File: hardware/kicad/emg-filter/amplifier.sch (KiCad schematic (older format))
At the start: 40 parts, among them U51 LM4565, U52 LM4565, U53 LM4565, U54 LM4565, U55 LM4565, U56 LM4565, U57 LM4565, U58 LM4565

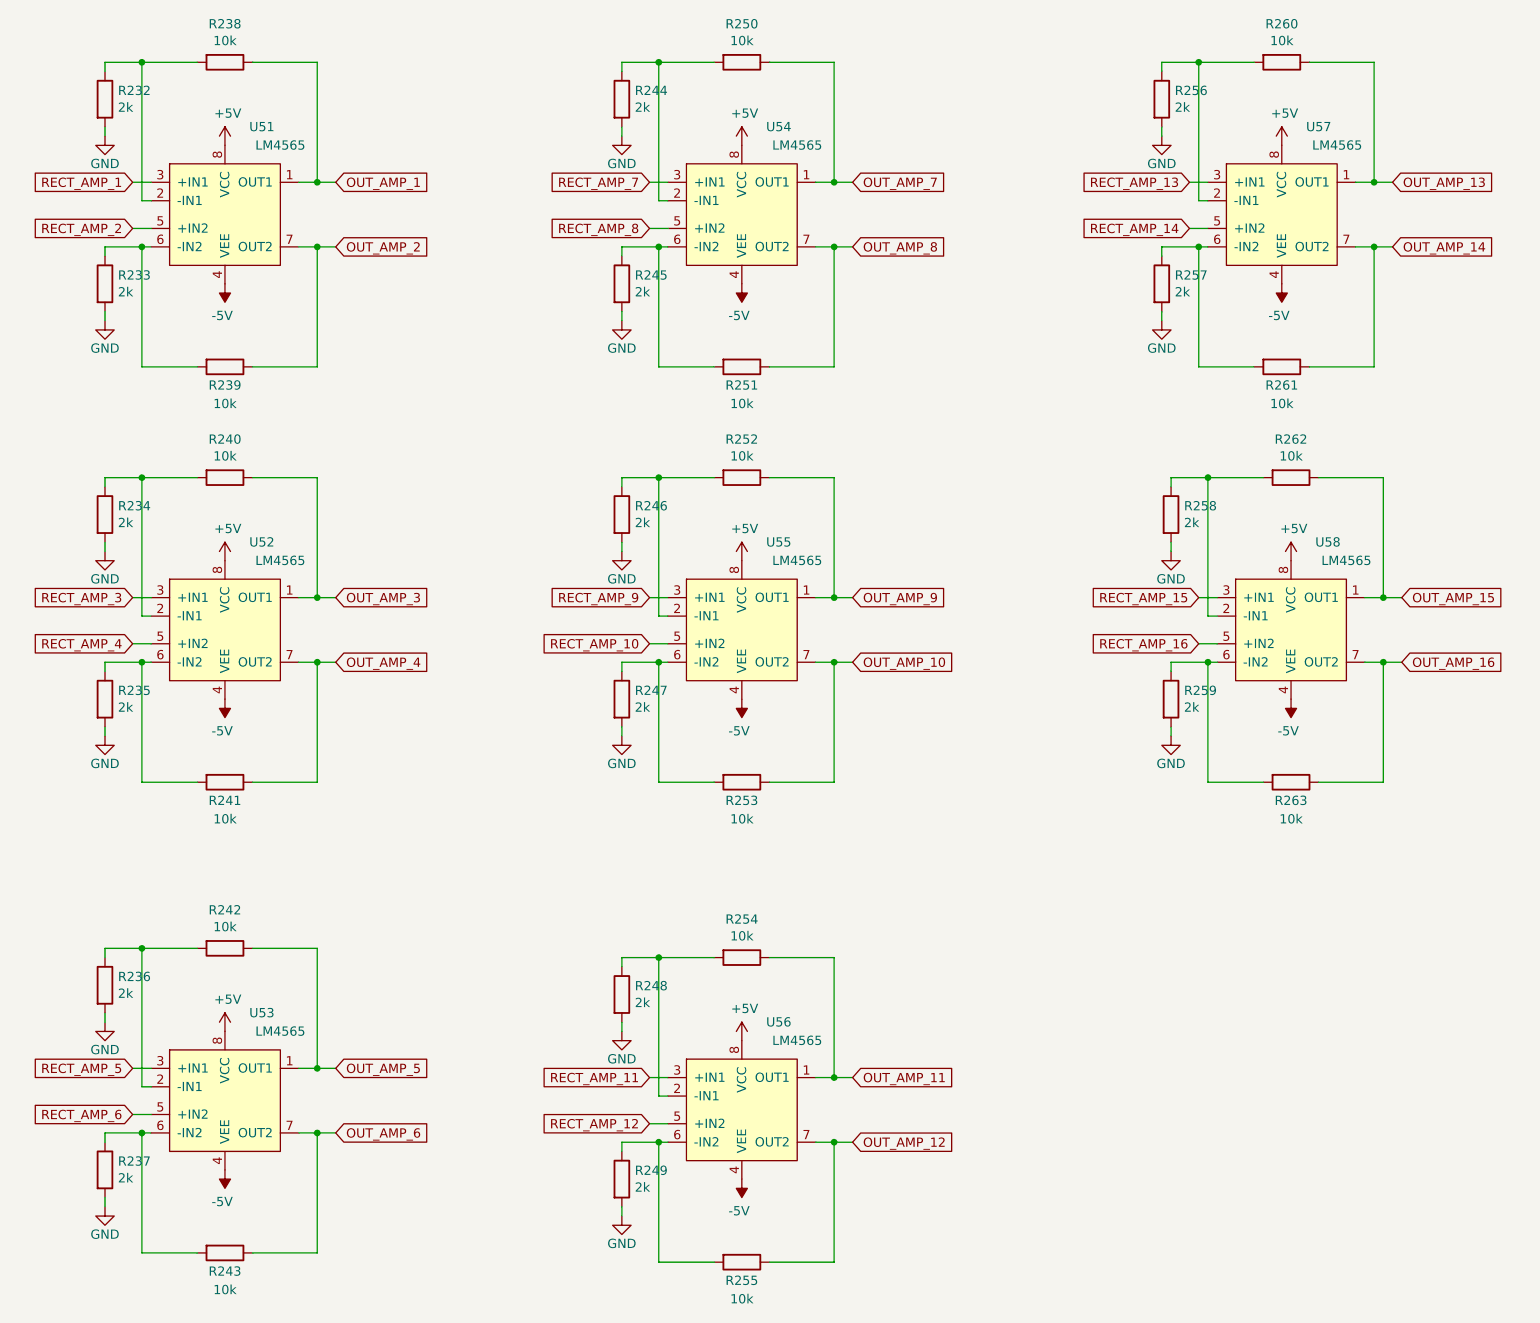
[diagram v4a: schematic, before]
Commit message: footprint association
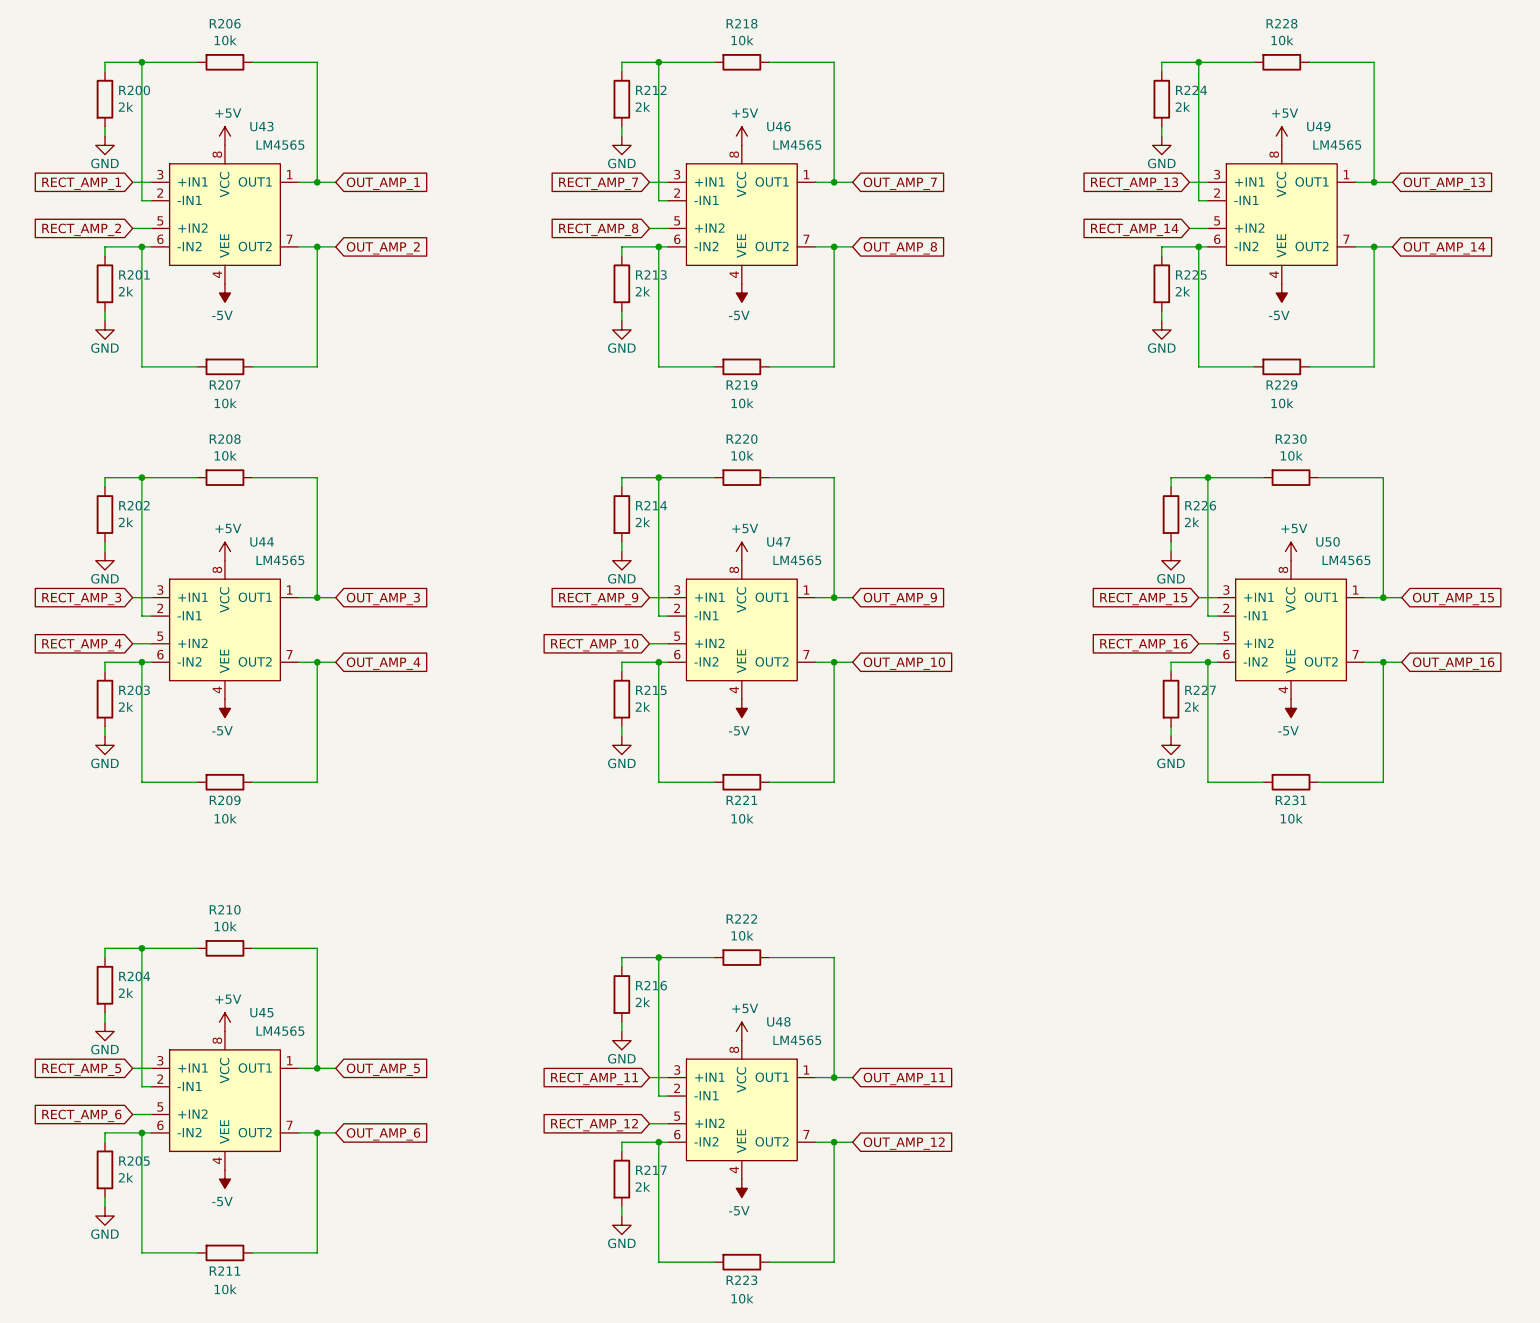
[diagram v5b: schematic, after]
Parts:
- R200: renamed from R232; footprint (none) -> Resistor_SMD:R_0805_2012Metric
- R201: renamed from R233; footprint (none) -> Resistor_SMD:R_0805_2012Metric
- R202: renamed from R234; footprint (none) -> Resistor_SMD:R_0805_2012Metric
- R203: renamed from R235; footprint (none) -> Resistor_SMD:R_0805_2012Metric
- R204: renamed from R236; footprint (none) -> Resistor_SMD:R_0805_2012Metric
- R205: renamed from R237; footprint (none) -> Resistor_SMD:R_0805_2012Metric
- R206: renamed from R238; footprint (none) -> Resistor_SMD:R_0805_2012Metric
- R207: renamed from R239; footprint (none) -> Resistor_SMD:R_0805_2012Metric
- R208: renamed from R240; footprint (none) -> Resistor_SMD:R_0805_2012Metric
- R209: renamed from R241; footprint (none) -> Resistor_SMD:R_0805_2012Metric
- R210: renamed from R242; footprint (none) -> Resistor_SMD:R_0805_2012Metric
- R211: renamed from R243; footprint (none) -> Resistor_SMD:R_0805_2012Metric
- R212: renamed from R244; footprint (none) -> Resistor_SMD:R_0805_2012Metric
- R213: renamed from R245; footprint (none) -> Resistor_SMD:R_0805_2012Metric
- R214: renamed from R246; footprint (none) -> Resistor_SMD:R_0805_2012Metric
- R215: renamed from R247; footprint (none) -> Resistor_SMD:R_0805_2012Metric
- R216: renamed from R248; footprint (none) -> Resistor_SMD:R_0805_2012Metric
- R217: renamed from R249; footprint (none) -> Resistor_SMD:R_0805_2012Metric
- R218: renamed from R250; footprint (none) -> Resistor_SMD:R_0805_2012Metric
- R219: renamed from R251; footprint (none) -> Resistor_SMD:R_0805_2012Metric
- R220: renamed from R252; footprint (none) -> Resistor_SMD:R_0805_2012Metric
- R221: renamed from R253; footprint (none) -> Resistor_SMD:R_0805_2012Metric
- R222: renamed from R254; footprint (none) -> Resistor_SMD:R_0805_2012Metric
- R223: renamed from R255; footprint (none) -> Resistor_SMD:R_0805_2012Metric
- R224: renamed from R256; footprint (none) -> Resistor_SMD:R_0805_2012Metric
- R225: renamed from R257; footprint (none) -> Resistor_SMD:R_0805_2012Metric
- R226: renamed from R258; footprint (none) -> Resistor_SMD:R_0805_2012Metric
- R227: renamed from R259; footprint (none) -> Resistor_SMD:R_0805_2012Metric
- R228: renamed from R260; footprint (none) -> Resistor_SMD:R_0805_2012Metric
- R229: renamed from R261; footprint (none) -> Resistor_SMD:R_0805_2012Metric
- R230: renamed from R262; footprint (none) -> Resistor_SMD:R_0805_2012Metric
- R231: renamed from R263; footprint (none) -> Resistor_SMD:R_0805_2012Metric
- renumbered U51 to U43, U52 to U44, U53 to U45, U54 to U46, U55 to U47, U56 to U48, U57 to U49, U58 to U50

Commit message: Solving Stuff for Free
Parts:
- renumbered R200 to R232, R201 to R233, R202 to R234, R203 to R235, R204 to R236, R205 to R237, R206 to R238, R207 to R239, R208 to R240, R209 to R241, R210 to R242, R211 to R243, R212 to R244, R213 to R245, R214 to R246, R215 to R247, R216 to R248, R217 to R249, R218 to R250, R219 to R251, R220 to R252, R221 to R253, R222 to R254, R223 to R255, R224 to R256, R225 to R257, R226 to R258, R227 to R259, R228 to R260, R229 to R261, R230 to R262, R231 to R263

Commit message: pcb
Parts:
- U43, U44, U45, U46, U47, U48, U49, U50: footprint (none) -> emg-filter:LM4565
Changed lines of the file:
@@
 F 0 "U43" H 2000 2100 50  0000 C CNN
 F 1 "LM4565" H 2100 2000 50  0000 C CNN
-F 2 "" H 2800 1650 50  0001 C CNN
+F 2 "emg-filter:LM4565" H 2800 1650 50  0001 C CNN
 F 3 "" H 2800 1650 50  0001 C CNN
 	1    1800 1650
@@
 F 0 "U44" H 2000 4350 50  0000 C CNN
 F 1 "LM4565" H 2100 4250 50  0000 C CNN
-F 2 "" H 2800 3900 50  0001 C CNN
+F 2 "emg-filter:LM4565" H 2800 3900 50  0001 C CNN
 F 3 "" H 2800 3900 50  0001 C CNN
 	1    1800 3900
@@
 F 0 "U46" H 4800 2100 50  0000 C CNN
 F 1 "LM4565" H 4900 2000 50  0000 C CNN
-F 2 "" H 5600 1650 50  0001 C CNN
+F 2 "emg-filter:LM4565" H 5600 1650 50  0001 C CNN
 F 3 "" H 5600 1650 50  0001 C CNN
 	1    4600 1650
@@
 F 0 "U47" H 4800 4350 50  0000 C CNN
 F 1 "LM4565" H 4900 4250 50  0000 C CNN
-F 2 "" H 5600 3900 50  0001 C CNN
+F 2 "emg-filter:LM4565" H 5600 3900 50  0001 C CNN
 F 3 "" H 5600 3900 50  0001 C CNN
 	1    4600 3900
@@
 F 0 "U49" H 7725 2100 50  0000 C CNN
 F 1 "LM4565" H 7825 2000 50  0000 C CNN
-F 2 "" H 8525 1650 50  0001 C CNN
+F 2 "emg-filter:LM4565" H 8525 1650 50  0001 C CNN
 F 3 "" H 8525 1650 50  0001 C CNN
 	1    7525 1650
@@
 F 0 "U50" H 7775 4350 50  0000 C CNN
 F 1 "LM4565" H 7875 4250 50  0000 C CNN
-F 2 "" H 8575 3900 50  0001 C CNN
+F 2 "emg-filter:LM4565" H 8575 3900 50  0001 C CNN
 F 3 "" H 8575 3900 50  0001 C CNN
 	1    7575 3900
@@
 F 0 "U45" H 2000 6900 50  0000 C CNN
 F 1 "LM4565" H 2100 6800 50  0000 C CNN
-F 2 "" H 2800 6450 50  0001 C CNN
+F 2 "emg-filter:LM4565" H 2800 6450 50  0001 C CNN
 F 3 "" H 2800 6450 50  0001 C CNN
 	1    1800 6450
@@
 F 0 "U48" H 4800 6950 50  0000 C CNN
 F 1 "LM4565" H 4900 6850 50  0000 C CNN
-F 2 "" H 5600 6500 50  0001 C CNN
+F 2 "emg-filter:LM4565" H 5600 6500 50  0001 C CNN
 F 3 "" H 5600 6500 50  0001 C CNN
 	1    4600 6500
